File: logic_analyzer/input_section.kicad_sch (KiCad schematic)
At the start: 23 parts, among them U1 ADA4891-4, U4 TLV3601

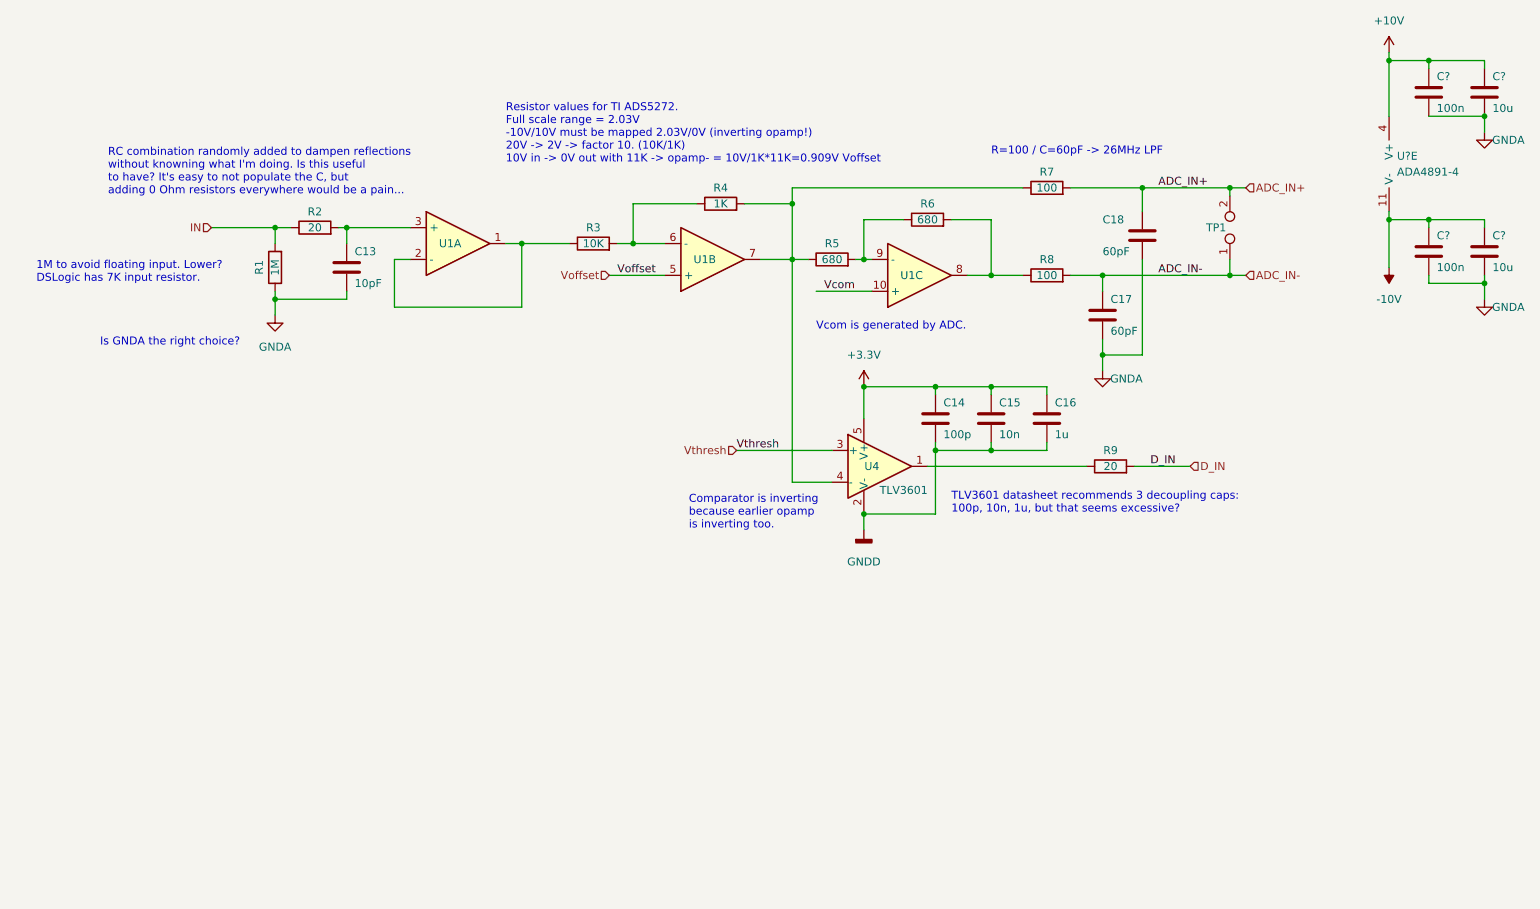
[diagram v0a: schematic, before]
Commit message: Update front-end with new values.
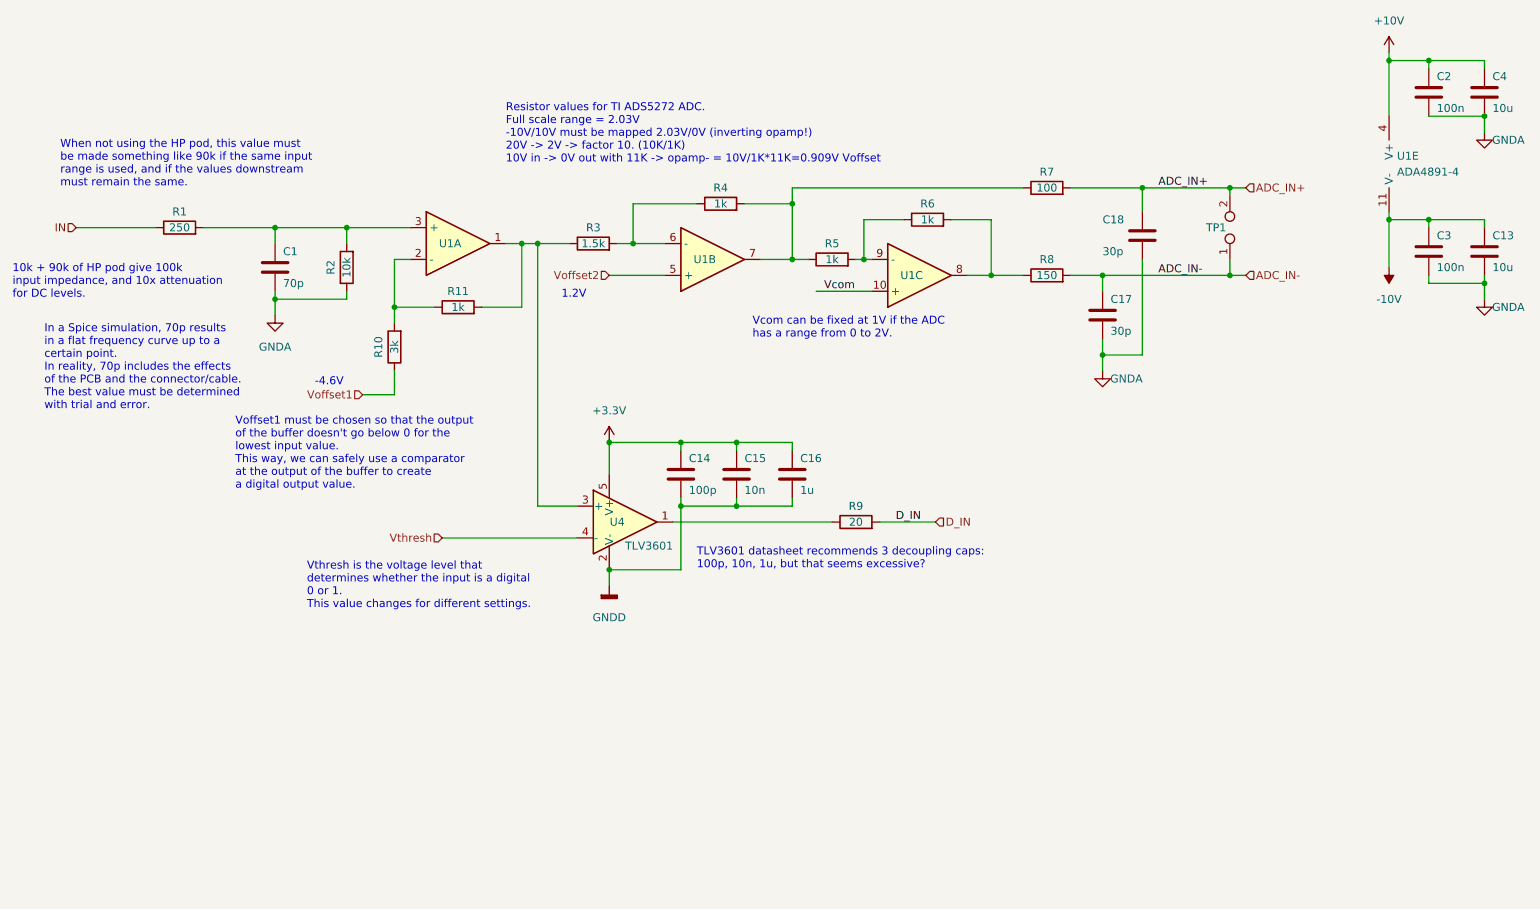
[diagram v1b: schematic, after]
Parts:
- removed C13: 10pF, symbol Device:C
- added C1: 70p, symbol Device:C
- added R10: 3k, symbol Device:R
- added R11: 1k, symbol Device:R
- C17, C18: value 60pF -> 30p
- R1: value 1M -> 250
- R2: value 20 -> 10k
- R3: value 10K -> 1.5k
- R4: value 1K -> 1k
- R5, R6: value 680 -> 1k
- R8: value 100 -> 150
- gave numbers to parts that had none: 5
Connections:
- net GNDA: now also R2.1, C1.2; no longer R1.1
- net IN: now also R1.1; no longer R1.2, R2.1
- net Vthresh: now also U4.4 (-); no longer U4.3 (+)
- net at R2.2, U1.3 (+): now also R1.2, C1.1
- net at R4.2, R5.1, R7.1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: no longer U4.4 (-)
- net at R3.1, U1.1: now also U4.3 (+), R11.2; no longer U1.2 (-)
- net Voffset renamed Voffset2
- new net: R10.2, R11.1, U1.2 (-)
- new net Voffset1: R10.1
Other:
- note added: "-4.6V"
- note added: "1.2V"
- note added: "10k + 90k of HP pod give 100k input impedance, and 10x attenuation for DC levels."
- note added: "In a Spice simulation, 70p results in a flat frequency curve up to a certain point. In reality, 70p includes the effects of the PCB and the connector/cable. The best value must be determined with trial and error."
- note added: "Resistor values for TI ADS5272 ADC. Full scale range = 2.03V -10V/10V must be mapped 2.03V/0V (inverting opamp!) 20V -> 2V -> factor 10. (10K/1K) 10V in -> 0V out with 11K -> opamp- = 10V/1K*11K=0.909V Voffset"
- note added: "Vcom can be fixed at 1V if the ADC has a range from 0 to 2V."
- note added: "Voffset1 must be chosen so that the output of the buffer doesn't go below 0 for the lowest input value. This way, we can safely use a comparator at the output of the buffer to create a digital output value."
- note added: "Vthresh is the voltage level that determines whether the input is a digital 0 or 1. This value changes for different settings."
- note added: "When not using the HP pod, this value must be made something like 90k if the same input range is used, and if the values downstream must remain the same."
- note removed: "1M to avoid floating input. Lower? DSLogic has 7K input resistor."
- note removed: "Comparator is inverting because earlier opamp is inverting too."
- note removed: "Is GNDA the right choice?"
- note removed: "R=100 / C=60pF -> 26MHz LPF"
- note removed: "RC combination randomly added to dampen reflections without knowning what I'm doing. Is this useful to have? It's easy to not populate the C, but adding 0 Ohm resistors everywhere would be a pain..."
- note removed: "Resistor values for TI ADS5272. Full scale range = 2.03V -10V/10V must be mapped 2.03V/0V (inverting opamp!) 20V -> 2V -> factor 10. (10K/1K) 10V in -> 0V out with 11K -> opamp- = 10V/1K*11K=0.909V Voffset"
- note removed: "Vcom is generated by ADC."
- moved on the sheet: C14, C15, C16, R9, U4

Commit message: Front-end placement exercise.
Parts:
- removed C1: 70p, symbol Device:C
- removed R1: 250, symbol Device:R
- removed R11: 1k, symbol Device:R
- removed unit 1 of U1
- added C10, C8: 30p, Capacitor_SMD:C_0603_1608Metric_Pad1.08x0.95mm_HandSolder, symbol Device:C
- added C2: 100p, Capacitor_SMD:C_0603_1608Metric_Pad1.08x0.95mm_HandSolder, symbol Device:C
- added C4: 10n, Capacitor_SMD:C_0603_1608Metric_Pad1.08x0.95mm_HandSolder, symbol Device:C
- added C6: 1u, Capacitor_SMD:C_0603_1608Metric_Pad1.08x0.95mm_HandSolder, symbol Device:C
- added R13: 100, Resistor_SMD:R_0603_1608Metric_Pad0.98x0.95mm_HandSolder, symbol Device:R
- added R14: 150, Resistor_SMD:R_0603_1608Metric_Pad0.98x0.95mm_HandSolder, symbol Device:R
- added R4, R6: 1k, Resistor_SMD:R_0603_1608Metric_Pad0.98x0.95mm_HandSolder, symbol Device:R
- added R8: 20, Resistor_SMD:R_0603_1608Metric_Pad0.98x0.95mm_HandSolder, symbol Device:R
- added TP2: TestPoint_2Pole, TestPoint:TestPoint_2Pads_Pitch2.54mm_Drill0.8mm, symbol Connector:TestPoint_2Pole
- added U2: TLV3601, Package_TO_SOT_SMD:SOT-23-5, symbol logic_analyzer:TLV3601
- added unit 4 of U3
- added unit 3 of U3
- C1: renamed from C14; footprint (none) -> Capacitor_SMD:C_0603_1608Metric_Pad1.08x0.95mm_HandSolder
- C11: renamed from C2; footprint (none) -> Capacitor_SMD:C_0603_1608Metric_Pad1.08x0.95mm_HandSolder
- C12: renamed from C3; footprint (none) -> Capacitor_SMD:C_0603_1608Metric_Pad1.08x0.95mm_HandSolder
- C13: renamed from C4; footprint (none) -> Capacitor_SMD:C_0603_1608Metric_Pad1.08x0.95mm_HandSolder
- C14: renamed from C13; footprint (none) -> Capacitor_SMD:C_0603_1608Metric_Pad1.08x0.95mm_HandSolder
- C3: renamed from C15; footprint (none) -> Capacitor_SMD:C_0603_1608Metric_Pad1.08x0.95mm_HandSolder
- C5: renamed from C16; footprint (none) -> Capacitor_SMD:C_0603_1608Metric_Pad1.08x0.95mm_HandSolder
- C7: renamed from C17; footprint (none) -> Capacitor_SMD:C_0603_1608Metric_Pad1.08x0.95mm_HandSolder
- C9: renamed from C18; footprint (none) -> Capacitor_SMD:C_0603_1608Metric_Pad1.08x0.95mm_HandSolder
- R1: renamed from R3; footprint (none) -> Resistor_SMD:R_0603_1608Metric_Pad0.98x0.95mm_HandSolder
- R10: value 3k -> 1k; footprint (none) -> Resistor_SMD:R_0603_1608Metric_Pad0.98x0.95mm_HandSolder
- R11: renamed from R7; footprint (none) -> Resistor_SMD:R_0603_1608Metric_Pad0.98x0.95mm_HandSolder
- R12: renamed from R8; footprint (none) -> Resistor_SMD:R_0603_1608Metric_Pad0.98x0.95mm_HandSolder
- R2: value 10k -> 1.5k; footprint (none) -> Resistor_SMD:R_0603_1608Metric_Pad0.98x0.95mm_HandSolder
- R3: renamed from R4; footprint (none) -> Resistor_SMD:R_0603_1608Metric_Pad0.98x0.95mm_HandSolder
- R5: footprint (none) -> Resistor_SMD:R_0603_1608Metric_Pad0.98x0.95mm_HandSolder
- R7: renamed from R9; footprint (none) -> Resistor_SMD:R_0603_1608Metric_Pad0.98x0.95mm_HandSolder
- R9: renamed from R6; footprint (none) -> Resistor_SMD:R_0603_1608Metric_Pad0.98x0.95mm_HandSolder
- TP1: footprint (none) -> TestPoint:TestPoint_2Pads_Pitch2.54mm_Drill0.8mm
- U3: renamed from U1; footprint (none) -> Package_SO:TSSOP-14_4.4x5mm_P0.65mm
- renumbered U4 to U1
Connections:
- net +3.3V: now also C2.1, C4.1, C6.1, U2.5 (V+)
- net GNDA: now also C10.2, C8.2; no longer R2.1
- net GNDD: now also C2.2, C4.2, C6.2, U2.2 (V-)
- net Vcom: now also U3.5 (+), U3.10 (+); no longer U3.10 (+)
- net Voffset2: now also U3.3 (+), U3.12 (+); no longer U3.5 (+)
- net Vthresh: now also U2.4 (-)
- net at R2.2: now also R4.1, U3.13 (-)
- net at R10.2: now also R14.1, U3.8
- net BUF_OUT0: now reaches R1.1, U1.3 (+)
- net at R12.1, R9.2: now also U3.7; no longer U3.8
- net at R5.2, R9.1: now also U3.6 (-); no longer U3.9 (-)
- net at R1.2, R3.1: now also U3.2 (-); no longer U3.6 (-)
- net at R11.1, R3.2, R5.1: now also U3.1; no longer U3.7
- net +10V renamed +5VA
- net -10V renamed -5VA
- net ADC_IN+ renamed ADC_IN0+
- net ADC_IN0+: now also C10.1, R13.2, TP2.2
- net ADC_IN- renamed ADC_IN0-
- net ADC_IN0-: now also C8.1, R14.2, TP2.1
- net D_IN renamed DIG_OUT0
- net Voffset1: no longer names the net of R10.1
- net Voffset1: now also R6.2, U3.9 (-)
- new net: R13.1, R4.2, R6.1, U3.14
- new net: R8.1, U2.1
- new net BUF_OUT1: R2.1, U2.3 (+)
- new net DIG_OUT1: R8.2
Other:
- note removed: "-4.6V"
- note removed: "10k + 90k of HP pod give 100k input impedance, and 10x attenuation for DC levels."
- note removed: "In a Spice simulation, 70p results in a flat frequency curve up to a certain point. In reality, 70p includes the effects of the PCB and the connector/cable. The best value must be determined with trial and error."
- note removed: "Voffset1 must be chosen so that the output of the buffer doesn't go below 0 for the lowest input value. This way, we can safely use a comparator at the output of the buffer to create a digital output value."
- note removed: "When not using the HP pod, this value must be made something like 90k if the same input range is used, and if the values downstream must remain the same."
- moved on the sheet: C1, C3, C5, C7, C9, R1, R11, R12, R3, R5, R7, R9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

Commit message: Before switching to hierarchical sheets.
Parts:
- renumbered C11 to C59, C13 to C60, C9 to C61, C7 to C62, C12 to C63, C14 to C64, C1 to C65, C3 to C66, C5 to C67, C10 to C68, C8 to C69, C2 to C70, C4 to C71, C6 to C72, R11 to R75, R3 to R76, R9 to R77, R1 to R78, R5 to R79, R12 to R80, R7 to R81, R13 to R82, R4 to R83, R10 to R84, R2 to R85, R6 to R86, R14 to R87, R8 to R88, TP1 to TP7, TP2 to TP8, U3 to U12, U1 to U13, U2 to U14

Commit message: Unknown logic_analyzer changes.
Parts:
- C59, C60, C61, C62, C63, C64, C65, C66, C67, C68, C69, C70, C71, C72: footprint Capacitor_SMD:C_0603_1608Metric_Pad1.08x0.95mm_HandSolder -> Capacitor_SMD:C_0402_1005Metric
- R75, R76, R77, R78, R79, R80, R81, R82, R83, R84, R85, R86, R87, R88: footprint Resistor_SMD:R_0603_1608Metric_Pad0.98x0.95mm_HandSolder -> Resistor_SMD:R_0402_1005Metric
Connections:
- net OA3_out: now reaches R82.1, R83.2, R86.1, U12.14
- net OA4_out: now reaches R84.2, R87.1, U12.8
- net OA2_out: now reaches R77.2, R80.1, U12.7
- net OA1_out: now reaches R75.1, R76.2, R79.1, U12.1
